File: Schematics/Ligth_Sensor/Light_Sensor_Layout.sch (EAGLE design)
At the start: 9 parts, among them J1 RJ45

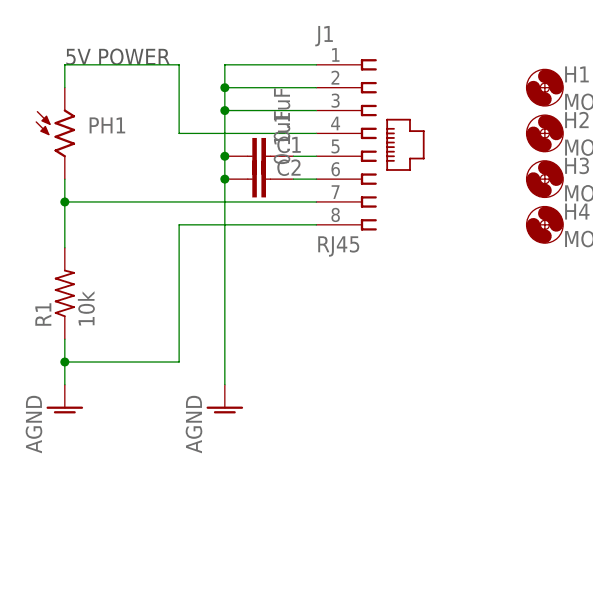
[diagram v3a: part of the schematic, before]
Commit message: Cleaned up stuff
Made Schematics easier to read
Split Supplies in BOM and made names match references
Renamed parts on sensor
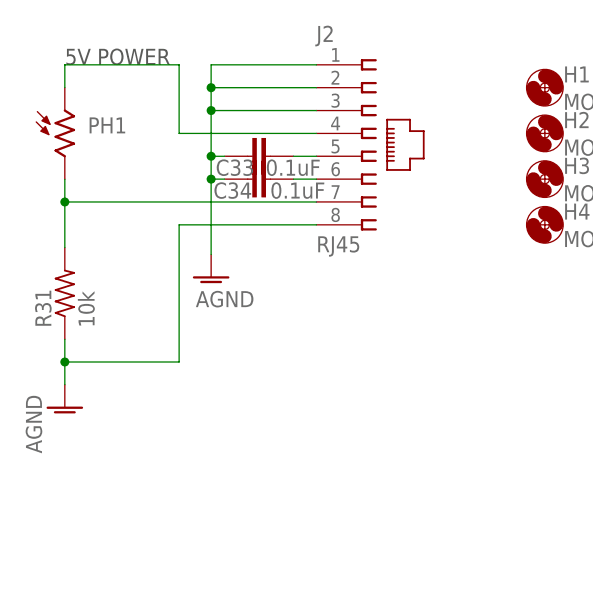
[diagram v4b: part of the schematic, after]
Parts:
- renumbered C1 to C33, C2 to C34, J1 to J2, R1 to R31
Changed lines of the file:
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@@
 <setting verticaltext="up"/>
 </settings>
-<grid distance="0.1" unitdist="inch" unit="inch" style="lines" multiple="1" display="no" altdistance="0.01" altunitdist="inch" altunit="inch"/>
+<grid distance="0.01" unitdist="inch" unit="inch" style="lines" multiple="1" display="no" altdistance="0.01" altunitdist="inch" altunit="inch"/>
 <layers>
 <layer number="1" name="Top" color="4" fill="1" visible="no" active="no"/>
@@
 <parts>
 <part name="PH1" library="photo-elements" deviceset="VT9" device="" technology="0N2" value="VT90N2"/>
-<part name="R1" library="rcl" deviceset="R-US_" device="R1206" value="10k"/>
-<part name="J1" library="con-amp" deviceset="555167-1" device="" value="RJ45"/>
+<part name="R31" library="rcl" deviceset="R-US_" device="R1206" value="10k"/>
+<part name="J2" library="con-amp" deviceset="555167-1" device="" value="RJ45"/>
 <part name="AGND1" library="supply1" deviceset="AGND" device=""/>
 <part name="AGND2" library="supply1" deviceset="AGND" device=""/>
@@
 <part name="H4" library="holes" deviceset="MOUNT-HOLE" device="2.8"/>
 <part name="FRAME1" library="frames" deviceset="FRAME_A_L" device="" value="4"/>
-<part name="C1" library="rcl" deviceset="C-EU" device="C0603K" value="0.1uF"/>
-<part name="C2" library="rcl" deviceset="C-EU" device="C0603K" value="0.1uF"/>
+<part name="C33" library="rcl" deviceset="C-EU" device="C0603K" value="0.1uF"/>
+<part name="C34" library="rcl" deviceset="C-EU" device="C0603K" value="0.1uF"/>
 </parts>
 <sheets>
@@
 <attribute name="NAME" x="88.9" y="55.88" size="1.778" layer="95"/>
 </instance>
-<instance part="R1" gate="G$1" x="86.36" y="38.1" rot="R90"/>
-<instance part="J1" gate="G$1" x="119.38" y="55.88"/>
+<instance part="R31" gate="G$1" x="86.36" y="38.1" rot="R90"/>
+<instance part="J2" gate="G$1" x="119.38" y="55.88"/>
 <instance part="AGND1" gate="VR1" x="86.36" y="25.4"/>
-<instance part="AGND2" gate="VR1" x="104.14" y="25.4"/>
+<instance part="AGND2" gate="VR1" x="102.616" y="39.878" smashed="yes">
+<attribute name="VALUE" x="107.442" y="38.354" size="1.778" layer="96" rot="R180"/>
+</instance>
 <instance part="H1" gate="G$1" x="139.7" y="60.96"/>
 <instance part="H2" gate="G$1" x="139.7" y="55.88"/>
@@
 <attribute name="SHEET" x="218.44" y="-34.29" size="2.54" layer="94" font="vector"/>
 </instance>
-<instance part="C1" gate="G$1" x="106.68" y="53.34" smashed="yes" rot="R90">
-<attribute name="NAME" x="112.776" y="55.499" size="1.778" layer="95" rot="R180"/>
-<attribute name="VALUE" x="111.379" y="54.864" size="1.778" layer="96" rot="R90"/>
+<instance part="C33" gate="G$1" x="106.68" y="53.34" smashed="yes" rot="R90">
+<attribute name="NAME" x="107.442" y="52.959" size="1.778" layer="95" rot="R180"/>
+<attribute name="VALUE" x="114.808" y="52.959" size="1.778" layer="96" rot="R180"/>
 </instance>
-<instance part="C2" gate="G$1" x="106.68" y="50.8" smashed="yes" rot="R90">
-<attribute name="NAME" x="112.776" y="52.959" size="1.778" layer="95" rot="R180"/>
-<attribute name="VALUE" x="111.379" y="52.324" size="1.778" layer="96" rot="R90"/>
+<instance part="C34" gate="G$1" x="106.68" y="50.8" smashed="yes" rot="R90">
+<attribute name="NAME" x="107.188" y="50.419" size="1.778" layer="95" rot="R180"/>
+<attribute name="VALUE" x="115.316" y="50.419" size="1.778" layer="96" rot="R180"/>
 </instance>
 </instances>
@@
 <wire x1="86.36" y1="63.5" x2="86.36" y2="60.96" width="0.1524" layer="91"/>
 <wire x1="99.06" y1="63.5" x2="99.06" y2="55.88" width="0.1524" layer="91"/>
-<pinref part="J1" gate="G$1" pin="4"/>
+<pinref part="J2" gate="G$1" pin="4"/>
 <wire x1="99.06" y1="55.88" x2="114.3" y2="55.88" width="0.1524" layer="91"/>
 </segment>
@@
 <segment>
 <pinref part="PH1" gate="G$1" pin="2"/>
-<pinref part="R1" gate="G$1" pin="2"/>
+<pinref part="R31" gate="G$1" pin="2"/>
 <wire x1="86.36" y1="50.8" x2="86.36" y2="48.26" width="0.1524" layer="91"/>
 <wire x1="86.36" y1="48.26" x2="86.36" y2="43.18" width="0.1524" layer="91"/>
 <wire x1="86.36" y1="48.26" x2="114.3" y2="48.26" width="0.1524" layer="91"/>
 <junction x="86.36" y="48.26"/>
-<pinref part="J1" gate="G$1" pin="7"/>
+<pinref part="J2" gate="G$1" pin="7"/>
 </segment>
 </net>
 <net name="AGND" class="0">
 <segment>
-<pinref part="R1" gate="G$1" pin="1"/>
+<pinref part="R31" gate="G$1" pin="1"/>
 <wire x1="86.36" y1="33.02" x2="86.36" y2="30.48" width="0.1524" layer="91"/>
 <wire x1="86.36" y1="30.48" x2="86.36" y2="27.94" width="0.1524" layer="91"/>
@@
 <pinref part="AGND1" gate="VR1" pin="AGND"/>
 <wire x1="99.06" y1="30.48" x2="99.06" y2="45.72" width="0.1524" layer="91"/>
-<pinref part="J1" gate="G$1" pin="8"/>
+<pinref part="J2" gate="G$1" pin="8"/>
 <wire x1="99.06" y1="45.72" x2="114.3" y2="45.72" width="0.1524" layer="91"/>
 </segment>
 <segment>
+<pinref part="J2" gate="G$1" pin="1"/>
+<wire x1="114.3" y1="63.5" x2="102.616" y2="63.5" width="0.1524" layer="91"/>
+<wire x1="102.616" y1="63.5" x2="102.616" y2="60.96" width="0.1524" layer="91"/>
+<pinref part="J2" gate="G$1" pin="2"/>
+<wire x1="102.616" y1="60.96" x2="102.616" y2="58.42" width="0.1524" layer="91"/>
+<wire x1="114.3" y1="60.96" x2="102.616" y2="60.96" width="0.1524" layer="91"/>
+<junction x="102.616" y="60.96"/>
+<pinref part="J2" gate="G$1" pin="3"/>
+<wire x1="114.3" y1="58.42" x2="102.616" y2="58.42" width="0.1524" layer="91"/>
+<wire x1="102.616" y1="42.418" x2="102.616" y2="50.8" width="0.1524" layer="91"/>
+<junction x="102.616" y="58.42"/>
 <pinref part="AGND2" gate="VR1" pin="AGND"/>
-<wire x1="104.14" y1="58.42" x2="104.14" y2="53.34" width="0.1524" layer="91"/>
-<pinref part="J1" gate="G$1" pin="1"/>
-<wire x1="104.14" y1="53.34" x2="104.14" y2="50.8" width="0.1524" layer="91"/>
-<wire x1="104.14" y1="50.8" x2="104.14" y2="27.94" width="0.1524" layer="91"/>
-<wire x1="114.3" y1="63.5" x2="104.14" y2="63.5" width="0.1524" layer="91"/>
-<wire x1="104.14" y1="63.5" x2="104.14" y2="60.96" width="0.1524" layer="91"/>
-<pinref part="J1" gate="G$1" pin="2"/>
-<wire x1="104.14" y1="60.96" x2="104.14" y2="58.42" width="0.1524" layer="91"/>
-<wire x1="114.3" y1="60.96" x2="104.14" y2="60.96" width="0.1524" layer="91"/>
-<junction x="104.14" y="60.96"/>
-<pinref part="J1" gate="G$1" pin="3"/>
-<wire x1="114.3" y1="58.42" x2="104.14" y2="58.42" width="0.1524" layer="91"/>
-<junction x="104.14" y="58.42"/>
-<pinref part="C1" gate="G$1" pin="1"/>
-<junction x="104.14" y="53.34"/>
-<pinref part="C2" gate="G$1" pin="1"/>
-<junction x="104.14" y="50.8"/>
+<pinref part="C33" gate="G$1" pin="1"/>
+<wire x1="102.616" y1="50.8" x2="102.616" y2="53.34" width="0.1524" layer="91"/>
+<wire x1="102.616" y1="53.34" x2="102.616" y2="58.42" width="0.1524" layer="91"/>
+<wire x1="104.14" y1="53.34" x2="102.616" y2="53.34" width="0.1524" layer="91"/>
+<junction x="102.616" y="53.34"/>
+<junction x="102.616" y="50.8"/>
+<pinref part="C34" gate="G$1" pin="1"/>
+<wire x1="104.14" y1="50.8" x2="102.616" y2="50.8" width="0.1524" layer="91"/>
 </segment>
 </net>
 <net name="N$23" class="0">
 <segment>
-<pinref part="J1" gate="G$1" pin="5"/>
+<pinref part="J2" gate="G$1" pin="5"/>
 <wire x1="114.3" y1="53.34" x2="111.76" y2="53.34" width="0.1524" layer="91"/>
-<pinref part="C1" gate="G$1" pin="2"/>
+<pinref part="C33" gate="G$1" pin="2"/>
 </segment>
 </net>
 <net name="N$24" class="0">
 <segment>
-<pinref part="J1" gate="G$1" pin="6"/>
+<pinref part="J2" gate="G$1" pin="6"/>
 <wire x1="114.3" y1="50.8" x2="111.76" y2="50.8" width="0.1524" layer="91"/>
-<pinref part="C2" gate="G$1" pin="2"/>
+<pinref part="C34" gate="G$1" pin="2"/>
 </segment>
 </net>
